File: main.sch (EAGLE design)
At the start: 31 parts, among them IC1 4050D, U1 MCP2551P-SOCKET, U2 STN1110SOCKET-28, Y1 16Mhz

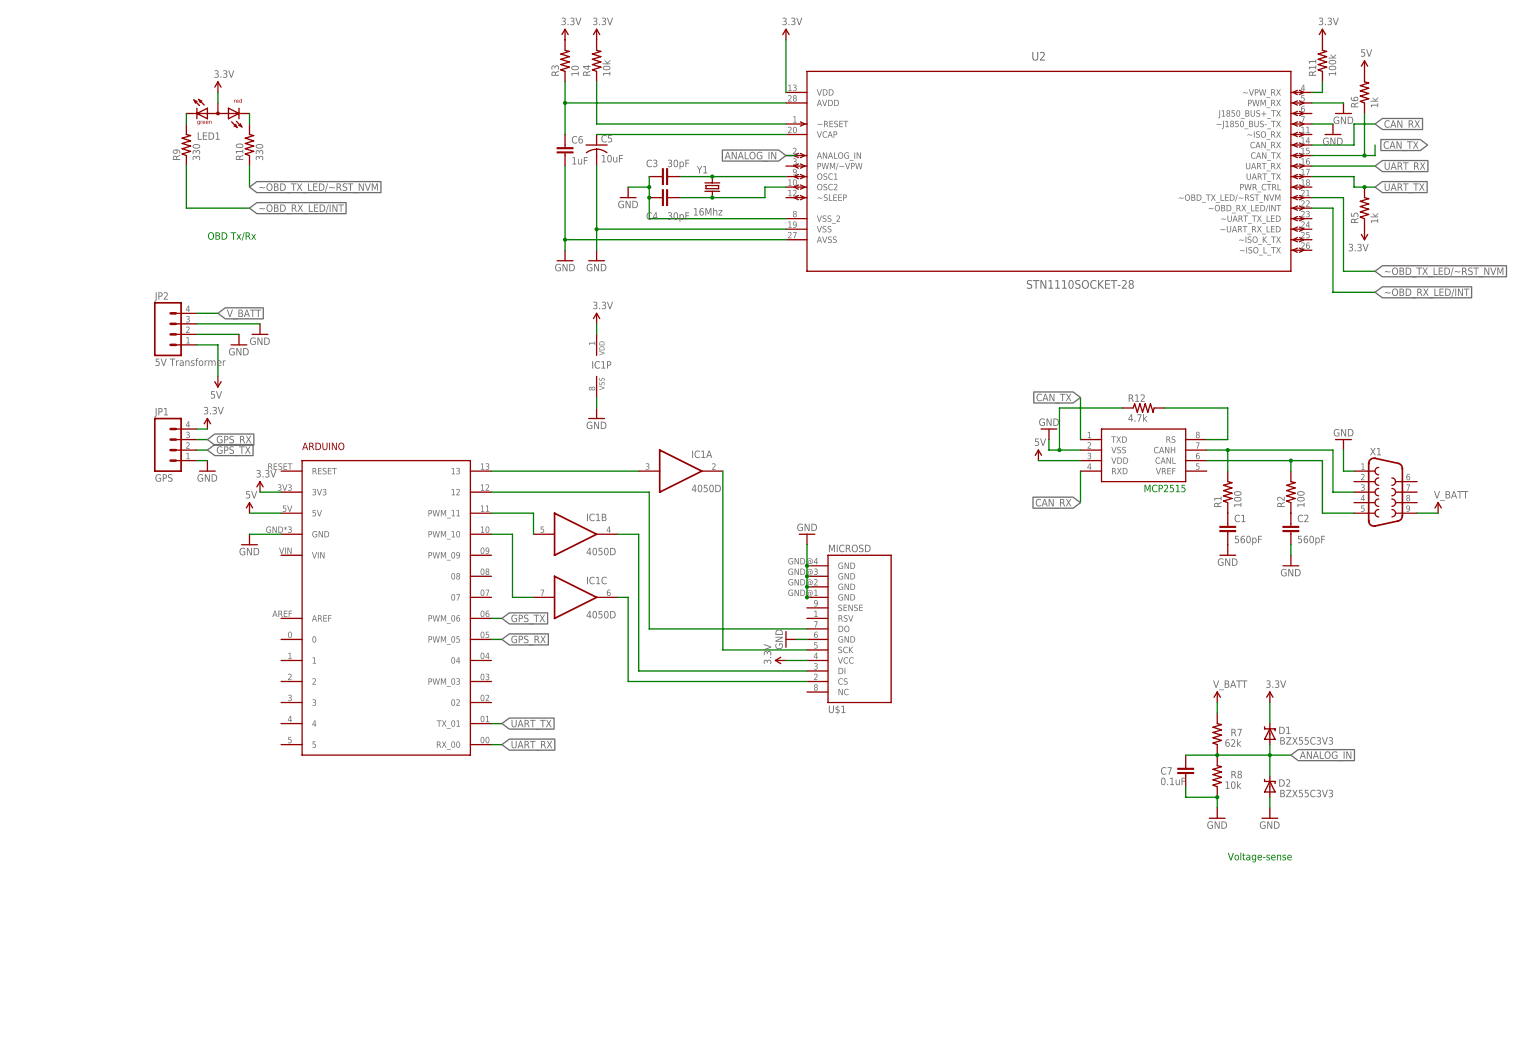
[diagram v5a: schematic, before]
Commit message: Reduced footprint, fixed DB9 connector
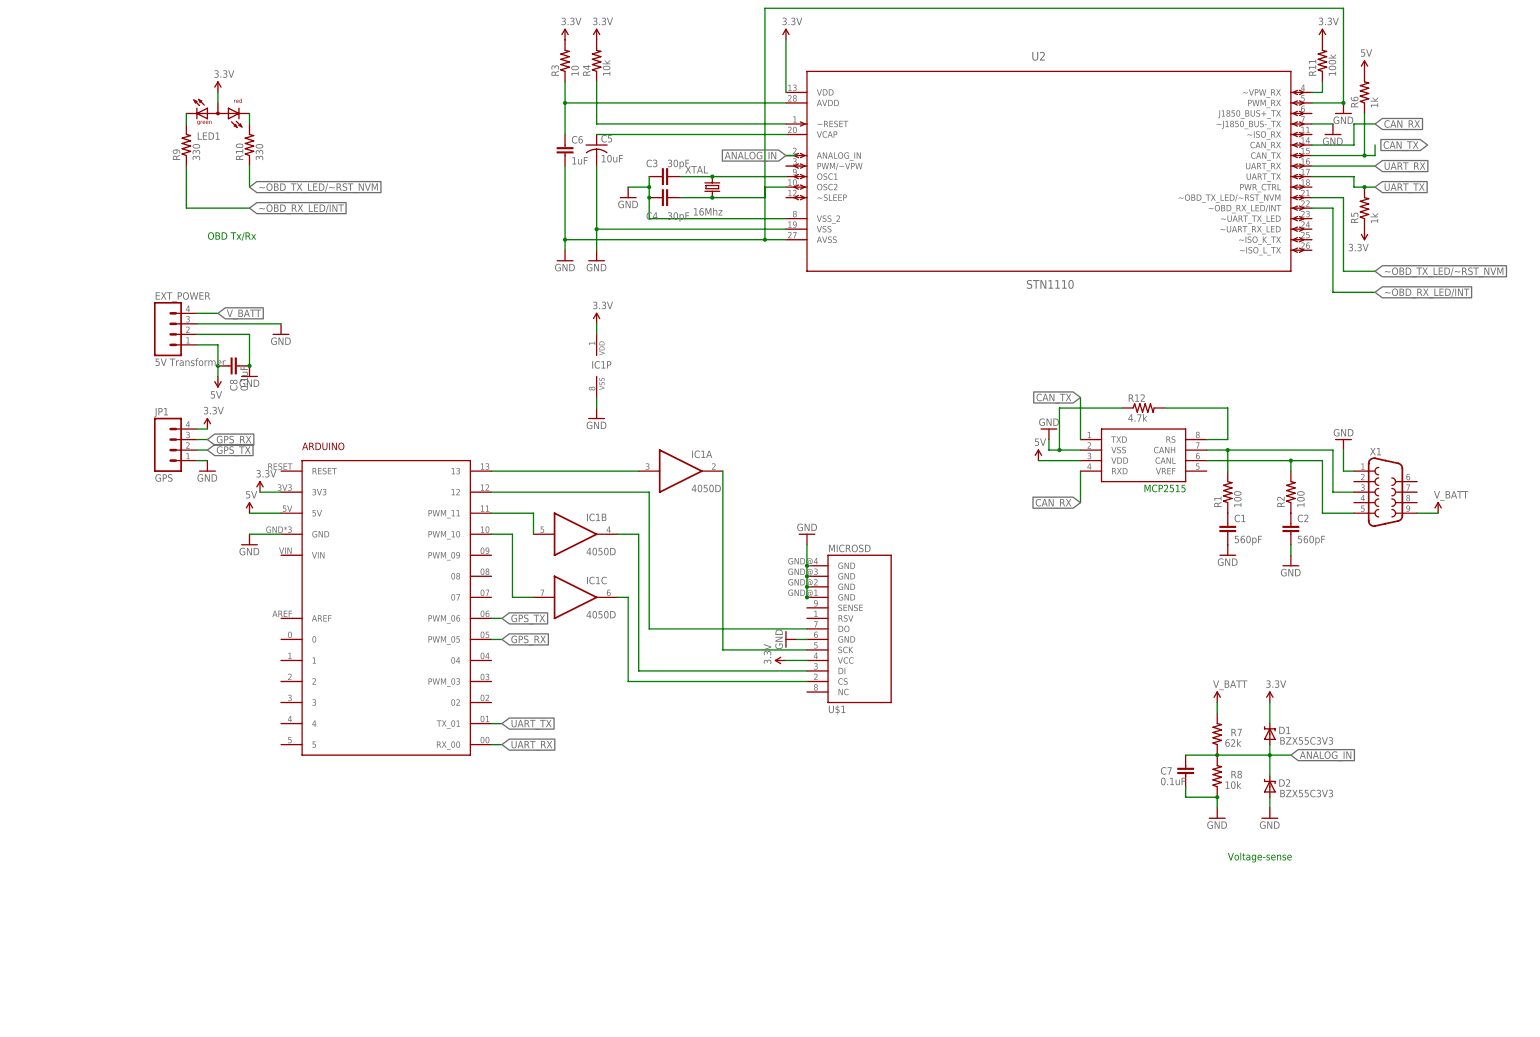
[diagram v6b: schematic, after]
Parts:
- added C8: 0.1uF, capacitor-wima:C2.5/2
- LED1: value L-115WEGW-CA -> OBD RX/TX
- U1: value MCP2551P-SOCKET -> MCP2551
- U2: value STN1110SOCKET-28 -> STN1110
- X1: device con-subd:F09HP -> SparkFun-Connectors:DB9MALE
- renumbered JP2 to EXT_POWER, Y1 to XTAL
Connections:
- net 5V: now also C8.1
- net GND: now also C8.2
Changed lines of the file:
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@@
 <parts>
 <part name="ARDUINO1" library="post7_arduino" deviceset="ARDUINO" device=""/>
-<part name="X1" library="con-subd" deviceset="F09" device="HP"/>
+<part name="X1" library="SparkFun-Connectors" deviceset="DB9" device="MALE"/>
 <part name="GND28" library="SparkFun" deviceset="GND" device=""/>
 <part name="GND15" library="SparkFun" deviceset="GND" device=""/>
-<part name="U1" library="personal" deviceset="MCP2551" device="P-SOCKET"/>
+<part name="U1" library="personal" deviceset="MCP2551" device="P-SOCKET" value="MCP2551"/>
 <part name="R1" library="resistor" deviceset="R-US_" device="0204/7" value="100"/>
 <part name="R2" library="resistor" deviceset="R-US_" device="0204/7" value="100"/>
@@
 <part name="SUPPLY2" library="SparkFun-Aesthetics" deviceset="5V" device=""/>
 <part name="SUPPLY3" library="SparkFun-Aesthetics" deviceset="3.3V" device=""/>
-<part name="U2" library="personal" deviceset="STN1110" device="SOCKET-28"/>
+<part name="U2" library="personal" deviceset="STN1110" device="SOCKET-28" value="STN1110"/>
 <part name="SUPPLY4" library="SparkFun-Aesthetics" deviceset="3.3V" device=""/>
 <part name="GND3" library="SparkFun-Aesthetics" deviceset="GND" device=""/>
 <part name="GND4" library="SparkFun-Aesthetics" deviceset="GND" device=""/>
 <part name="SUPPLY5" library="SparkFun-Aesthetics" deviceset="V_BATT" device=""/>
-<part name="Y1" library="SparkFun-FreqCtrl" deviceset="CRYSTAL" device="HC49UV" value="16Mhz"/>
+<part name="XTAL" library="SparkFun-FreqCtrl" deviceset="CRYSTAL" device="HC49UV" value="16Mhz"/>
 <part name="C3" library="capacitor-wima" deviceset="C" device="2.5/2" value="30pF"/>
 <part name="C4" library="capacitor-wima" deviceset="C" device="2.5/2" value="30pF"/>
@@
 <part name="R9" library="resistor" deviceset="R-US_" device="0204/7" value="330"/>
 <part name="R10" library="resistor" deviceset="R-US_" device="0204/7" value="330"/>
-<part name="LED1" library="led" deviceset="L-115WEGW-CA" device=""/>
+<part name="LED1" library="led" deviceset="L-115WEGW-CA" device="" value="OBD RX/TX"/>
 <part name="SUPPLY12" library="SparkFun-Aesthetics" deviceset="3.3V" device=""/>
 <part name="R11" library="resistor" deviceset="R-US_" device="0204/7" value="100k"/>
@@
 <part name="GND14" library="SparkFun-Aesthetics" deviceset="GND" device=""/>
 <part name="FRAME1" library="SparkFun-Aesthetics" deviceset="FRAME-A3" device=""/>
-<part name="JP2" library="SparkFun-Connectors" deviceset="M04" device="LOCK" value="5V Transformer"/>
+<part name="EXT_POWER" library="SparkFun-Connectors" deviceset="M04" device="LOCK" value="5V Transformer"/>
 <part name="GND16" library="SparkFun-Aesthetics" deviceset="GND" device=""/>
 <part name="GND17" library="SparkFun-Aesthetics" deviceset="GND" device=""/>
 <part name="SUPPLY17" library="SparkFun-Aesthetics" deviceset="5V" device=""/>
+<part name="C8" library="capacitor-wima" deviceset="C" device="2.5/2" value="0.1uF"/>
 </parts>
 <sheets>
@@
 <instance part="GND4" gate="1" x="190.5" y="78.74" rot="R180"/>
 <instance part="SUPPLY5" gate="G$1" x="284.48" y="58.42"/>
-<instance part="Y1" gate="G$1" x="109.22" y="137.16" smashed="yes" rot="R90">
+<instance part="XTAL" gate="G$1" x="109.22" y="137.16" smashed="yes" rot="R90">
 <attribute name="NAME" x="108.204" y="142.24" size="1.778" layer="95" rot="R180"/>
 <attribute name="VALUE" x="111.76" y="132.08" size="1.778" layer="96" rot="R180"/>
@@
 <instance part="GND14" gate="1" x="127" y="27.94" rot="R270"/>
 <instance part="FRAME1" gate="G$1" x="-73.66" y="-71.12"/>
-<instance part="JP2" gate="G$1" x="-20.32" y="101.6"/>
-<instance part="GND16" gate="1" x="-5.08" y="99.06"/>
-<instance part="GND17" gate="1" x="0" y="101.6"/>
+<instance part="EXT_POWER" gate="G$1" x="-20.32" y="101.6"/>
+<instance part="GND16" gate="1" x="-2.54" y="91.44"/>
+<instance part="GND17" gate="1" x="5.08" y="101.6"/>
 <instance part="SUPPLY17" gate="G$1" x="-10.16" y="91.44" rot="R180"/>
+<instance part="C8" gate="G$1" x="-7.62" y="93.98" smashed="yes" rot="R90">
+<attribute name="NAME" x="-5.461" y="87.884" size="1.778" layer="95" rot="R90"/>
+<attribute name="VALUE" x="-2.921" y="87.884" size="1.778" layer="96" rot="R90"/>
+</instance>
 </instances>
 <busses>
@@
 <segment>
 <pinref part="U2" gate="A" pin="AVSS"/>
-<wire x1="127" y1="124.46" x2="73.66" y2="124.46" width="0.1524" layer="91"/>
+<wire x1="127" y1="124.46" x2="121.92" y2="124.46" width="0.1524" layer="91"/>
 <pinref part="C6" gate="G$1" pin="2"/>
+<wire x1="121.92" y1="124.46" x2="73.66" y2="124.46" width="0.1524" layer="91"/>
 <wire x1="73.66" y1="142.24" x2="73.66" y2="124.46" width="0.1524" layer="91"/>
 <wire x1="73.66" y1="121.92" x2="73.66" y2="124.46" width="0.1524" layer="91"/>
 <pinref part="GND6" gate="1" pin="GND"/>
 <junction x="73.66" y="124.46"/>
+<wire x1="121.92" y1="124.46" x2="121.92" y2="180.34" width="0.1524" layer="91"/>
+<pinref part="U2" gate="A" pin="PWM_RX"/>
+<wire x1="254" y1="157.48" x2="261.62" y2="157.48" width="0.1524" layer="91"/>
+<pinref part="GND9" gate="1" pin="GND"/>
+<wire x1="121.92" y1="180.34" x2="261.62" y2="180.34" width="0.1524" layer="91"/>
+<wire x1="261.62" y1="180.34" x2="261.62" y2="157.48" width="0.1524" layer="91"/>
+<junction x="121.92" y="124.46"/>
+<junction x="261.62" y="157.48"/>
 </segment>
 <segment>
@@
 <wire x1="243.84" y1="-10.16" x2="243.84" y2="-12.7" width="0.1524" layer="91"/>
 <pinref part="GND8" gate="1" pin="GND"/>
-</segment>
-<segment>
-<pinref part="U2" gate="A" pin="PWM_RX"/>
-<wire x1="254" y1="157.48" x2="261.62" y2="157.48" width="0.1524" layer="91"/>
-<pinref part="GND9" gate="1" pin="GND"/>
 </segment>
 <segment>
@@
 </segment>
 <segment>
-<pinref part="JP2" gate="G$1" pin="2"/>
+<pinref part="EXT_POWER" gate="G$1" pin="2"/>
 <pinref part="GND16" gate="1" pin="GND"/>
-<wire x1="-15.24" y1="101.6" x2="-5.08" y2="101.6" width="0.1524" layer="91"/>
-</segment>
-<segment>
-<pinref part="JP2" gate="G$1" pin="3"/>
+<wire x1="-15.24" y1="101.6" x2="-2.54" y2="101.6" width="0.1524" layer="91"/>
+<wire x1="-2.54" y1="101.6" x2="-2.54" y2="93.98" width="0.1524" layer="91"/>
+<pinref part="C8" gate="G$1" pin="2"/>
+<junction x="-2.54" y="93.98"/>
+</segment>
+<segment>
+<pinref part="EXT_POWER" gate="G$1" pin="3"/>
 <pinref part="GND17" gate="1" pin="GND"/>
-<wire x1="-15.24" y1="104.14" x2="0" y2="104.14" width="0.1524" layer="91"/>
+<wire x1="-15.24" y1="104.14" x2="5.08" y2="104.14" width="0.1524" layer="91"/>
 </segment>
 </net>
@@
 </segment>
 <segment>
-<pinref part="JP2" gate="G$1" pin="1"/>
+<pinref part="EXT_POWER" gate="G$1" pin="1"/>
 <pinref part="SUPPLY17" gate="G$1" pin="5V"/>
 <wire x1="-15.24" y1="99.06" x2="-10.16" y2="99.06" width="0.1524" layer="91"/>
-<wire x1="-10.16" y1="99.06" x2="-10.16" y2="91.44" width="0.1524" layer="91"/>
+<wire x1="-10.16" y1="99.06" x2="-10.16" y2="93.98" width="0.1524" layer="91"/>
+<pinref part="C8" gate="G$1" pin="1"/>
+<wire x1="-10.16" y1="93.98" x2="-10.16" y2="91.44" width="0.1524" layer="91"/>
+<junction x="-10.16" y="93.98"/>
 </segment>
 </net>
@@
 </segment>
 <segment>
-<pinref part="JP2" gate="G$1" pin="4"/>
+<pinref part="EXT_POWER" gate="G$1" pin="4"/>
 <wire x1="-15.24" y1="106.68" x2="-10.16" y2="106.68" width="0.1524" layer="91"/>
 <label x="-10.16" y="106.68" size="1.778" layer="95" xref="yes"/>
@@
 <pinref part="C3" gate="G$1" pin="2"/>
 <wire x1="127" y1="139.7" x2="109.22" y2="139.7" width="0.1524" layer="91"/>
-<pinref part="Y1" gate="G$1" pin="2"/>
+<pinref part="XTAL" gate="G$1" pin="2"/>
 <junction x="109.22" y="139.7"/>
 <wire x1="109.22" y1="139.7" x2="101.6" y2="139.7" width="0.1524" layer="91"/>
@@
 <wire x1="121.92" y1="134.62" x2="109.22" y2="134.62" width="0.1524" layer="91"/>
 <pinref part="C4" gate="G$1" pin="2"/>
-<pinref part="Y1" gate="G$1" pin="1"/>
+<pinref part="XTAL" gate="G$1" pin="1"/>
 <junction x="109.22" y="134.62"/>
 <wire x1="109.22" y1="134.62" x2="101.6" y2="134.62" width="0.1524" layer="91"/>

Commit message: Review phase 1
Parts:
- added R13: 100k, resistor:R-US_0204/7
- U2: value STN1110 -> STN1100
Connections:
- net 3.3V: now also R13.1
- net GND: now also U2.~ISO_RX; no longer U2.~J1850_BUS-_TX
- net ~OBD_TX_LED/~RST_NVM: now also R13.2
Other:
- moved on the sheet: R5
